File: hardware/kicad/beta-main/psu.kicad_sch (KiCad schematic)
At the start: 34 parts, among them J18 XT60, U5 AP3441SHE-7B, U6 TPS56624x, U7 AP2553W6

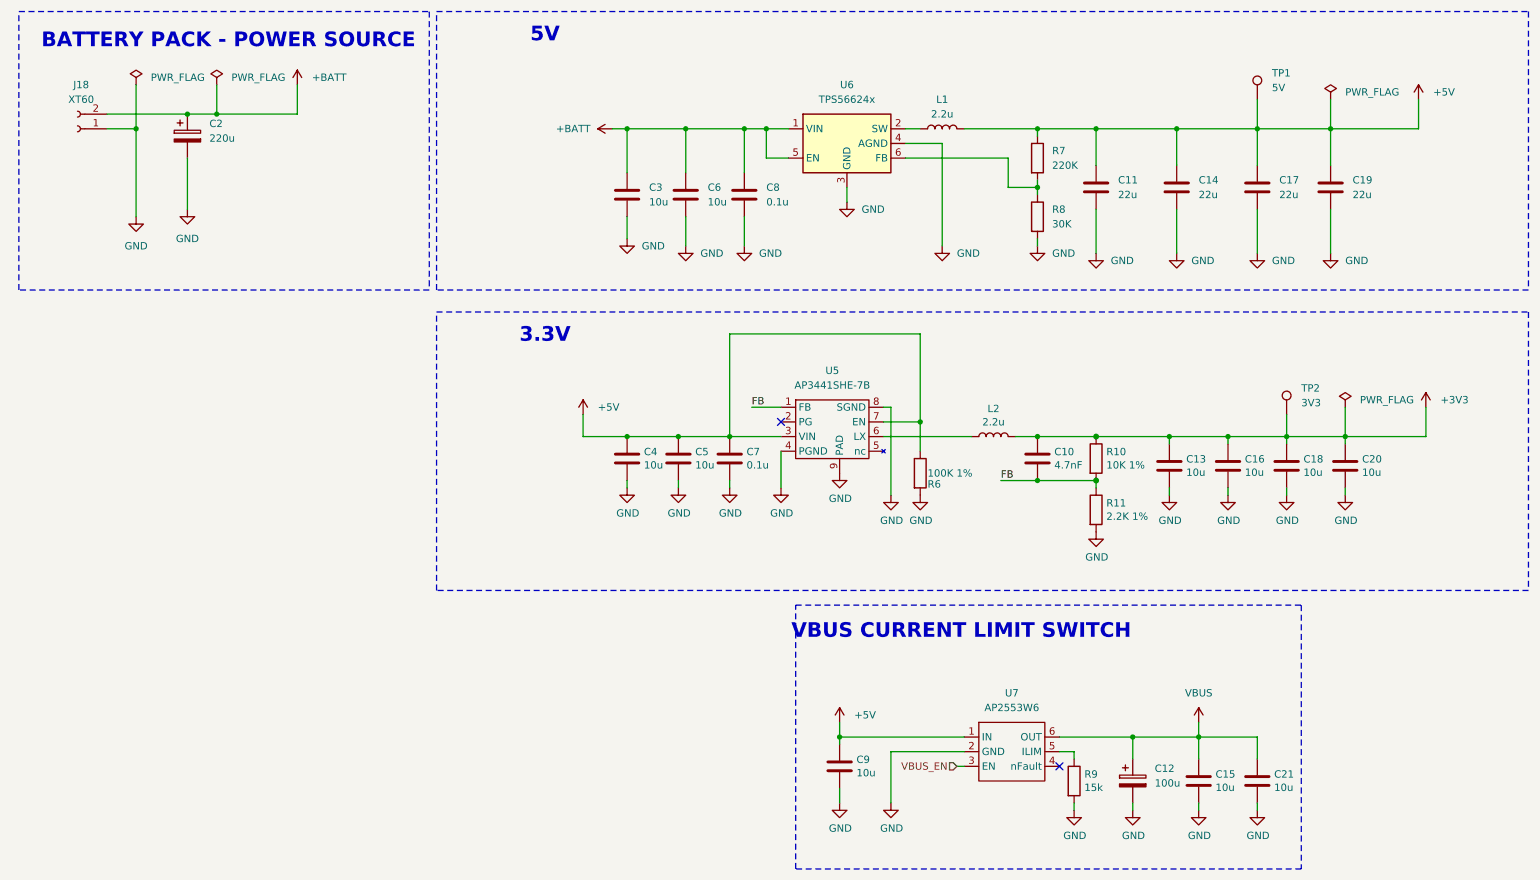
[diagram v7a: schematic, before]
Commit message: BOM, all easily found parts from digi
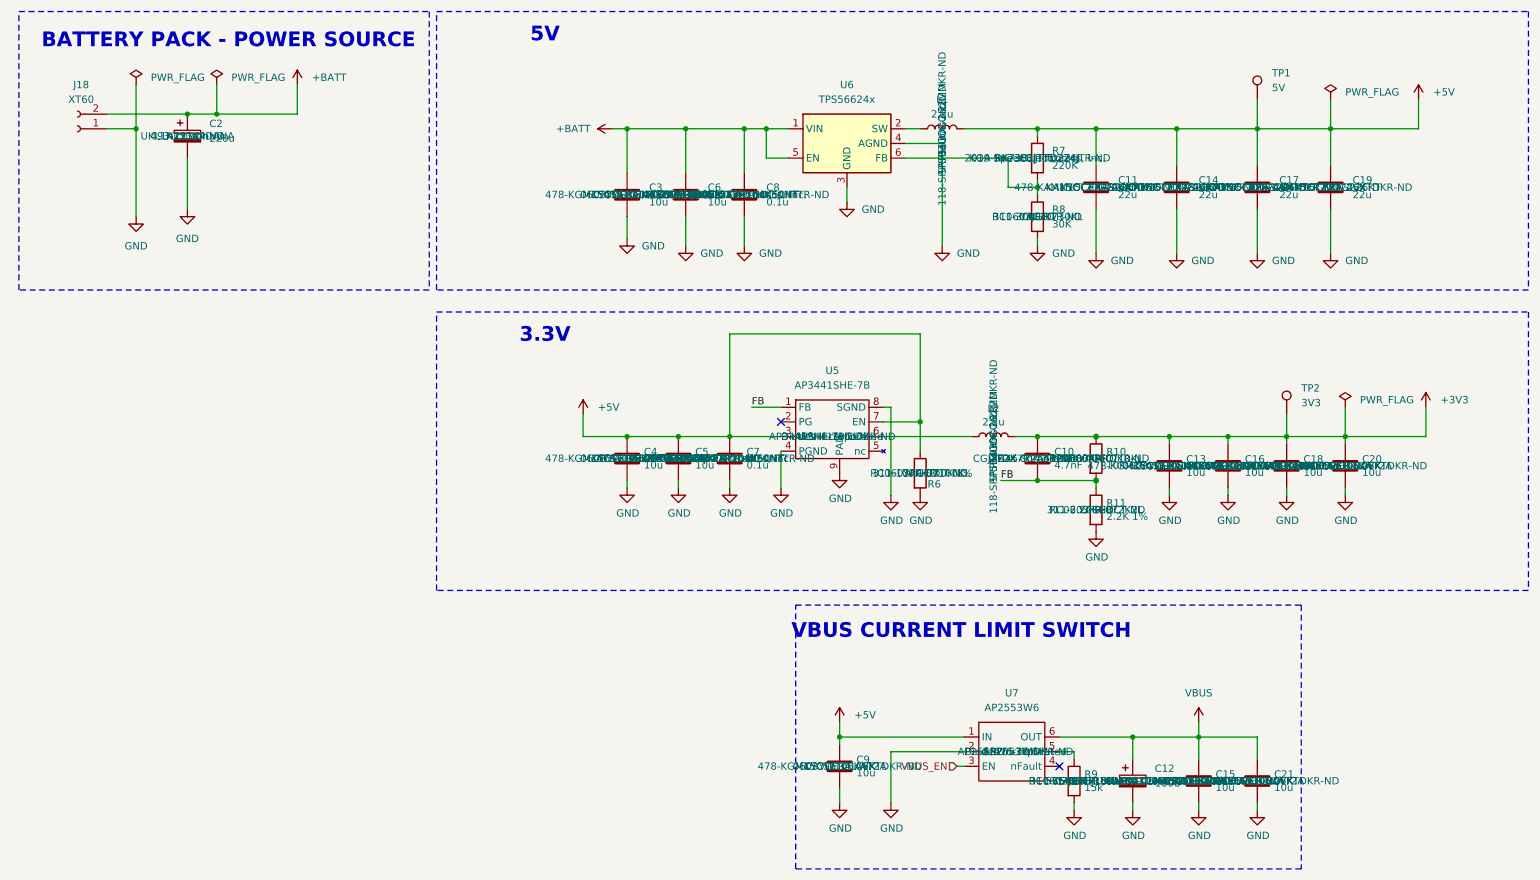
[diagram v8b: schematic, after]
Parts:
- C10: DigiKey_Part_Number (none) -> 445-9141-2-ND; MANUFACTURER (none) -> TDK Corporation; MP (none) -> CGJ3E2X7R2A472K080AA
- C11, C14, C17, C19: DigiKey_Part_Number (none) -> 478-KAM15CT70G226KTDKR-ND; MANUFACTURER (none) -> KYOCERA AVX; MP (none) -> KAM15CT70G226KT
- C12: footprint Capacitor_SMD:CP_Elec_6.3x5.9 -> Capacitor_SMD:CP_Elec_6.3x7.7; DigiKey_Part_Number (none) -> 565-EMHJ160ARA101MF80GTR-ND; MANUFACTURER (none) -> Chemi-Con; MP (none) -> EMHJ160ARA101MF80G
- C13, C15, C16, C18, C20, C21, C3, C4, C5, C6, C9: DigiKey_Part_Number (none) -> 478-KGM15CS61C106KTDKR-ND; MANUFACTURER (none) -> KYOCERA AVX; MP (none) -> 0603YW106KAT2A
- C2: footprint (none) -> Capacitor_THT:CP_Radial_D8.0mm_P3.50mm; DigiKey_Part_Number (none) -> 493-15344-ND; MANUFACTURER (none) -> Nichicon; MP (none) -> UKL1A221KPDANA
- C7, C8: DigiKey_Part_Number (none) -> 2571-GMC10X7R104K50NTTR-ND; MANUFACTURER (none) -> Cal-Chip Electronics, Inc.; MP (none) -> GMC10X7R104K50NT
- L1, L2: DigiKey_Part_Number (none) -> 118-SRP5030CC-2R2MDKR-ND; MANUFACTURER (none) -> Bourns Inc.; MP (none) -> SRP5030CC-2R2M
- R10: DigiKey_Part_Number (none) -> 311-10.0KHRDKR-ND; MANUFACTURER (none) -> YAGEO; MP (none) -> RC0603FR-0710KL
- R11: DigiKey_Part_Number (none) -> 311-2.20KHRCT-ND; MANUFACTURER (none) -> YAGEO; MP (none) -> RC0603FR-072K2L
- R6: DigiKey_Part_Number (none) -> 311-100KHRCT-ND; MANUFACTURER (none) -> YAGEO; MP (none) -> RC0603FR-07100KL
- R7: DigiKey_Part_Number (none) -> 2019-RK73B1JTTD224JTR-ND; MANUFACTURER (none) -> KOA Speer Electronics, Inc.; MP (none) -> RK73B1JTTD224J
- R8: DigiKey_Part_Number (none) -> 311-30KGRTR-ND; MANUFACTURER (none) -> YAGEO; MP (none) -> RC0603JR-0730KL
- R9: DigiKey_Part_Number (none) -> 311-15KGRTR-ND; MANUFACTURER (none) -> YAGEO; MP (none) -> RC0603JR-0715KL
- U5: DigiKey_Part_Number (none) -> AP3441SHE-7BDIDKR-ND; MANUFACTURER (none) -> Diodes Incorporated; MP (none) -> AP3441SHE-7B
- U7: DigiKey_Part_Number (none) -> AP2553W6-7DIDKR-ND; MANUFACTURER (none) -> Diodes Incorporated; MP (none) -> AP2553W6-7
